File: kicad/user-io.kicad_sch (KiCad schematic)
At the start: 26 parts, among them J1 USB1, SW1 PTS815, U1 MIMXRT1171DVMAB, U2 MAYA-W166-00B, U3 LSM6DSV, U4 LIS2MDL

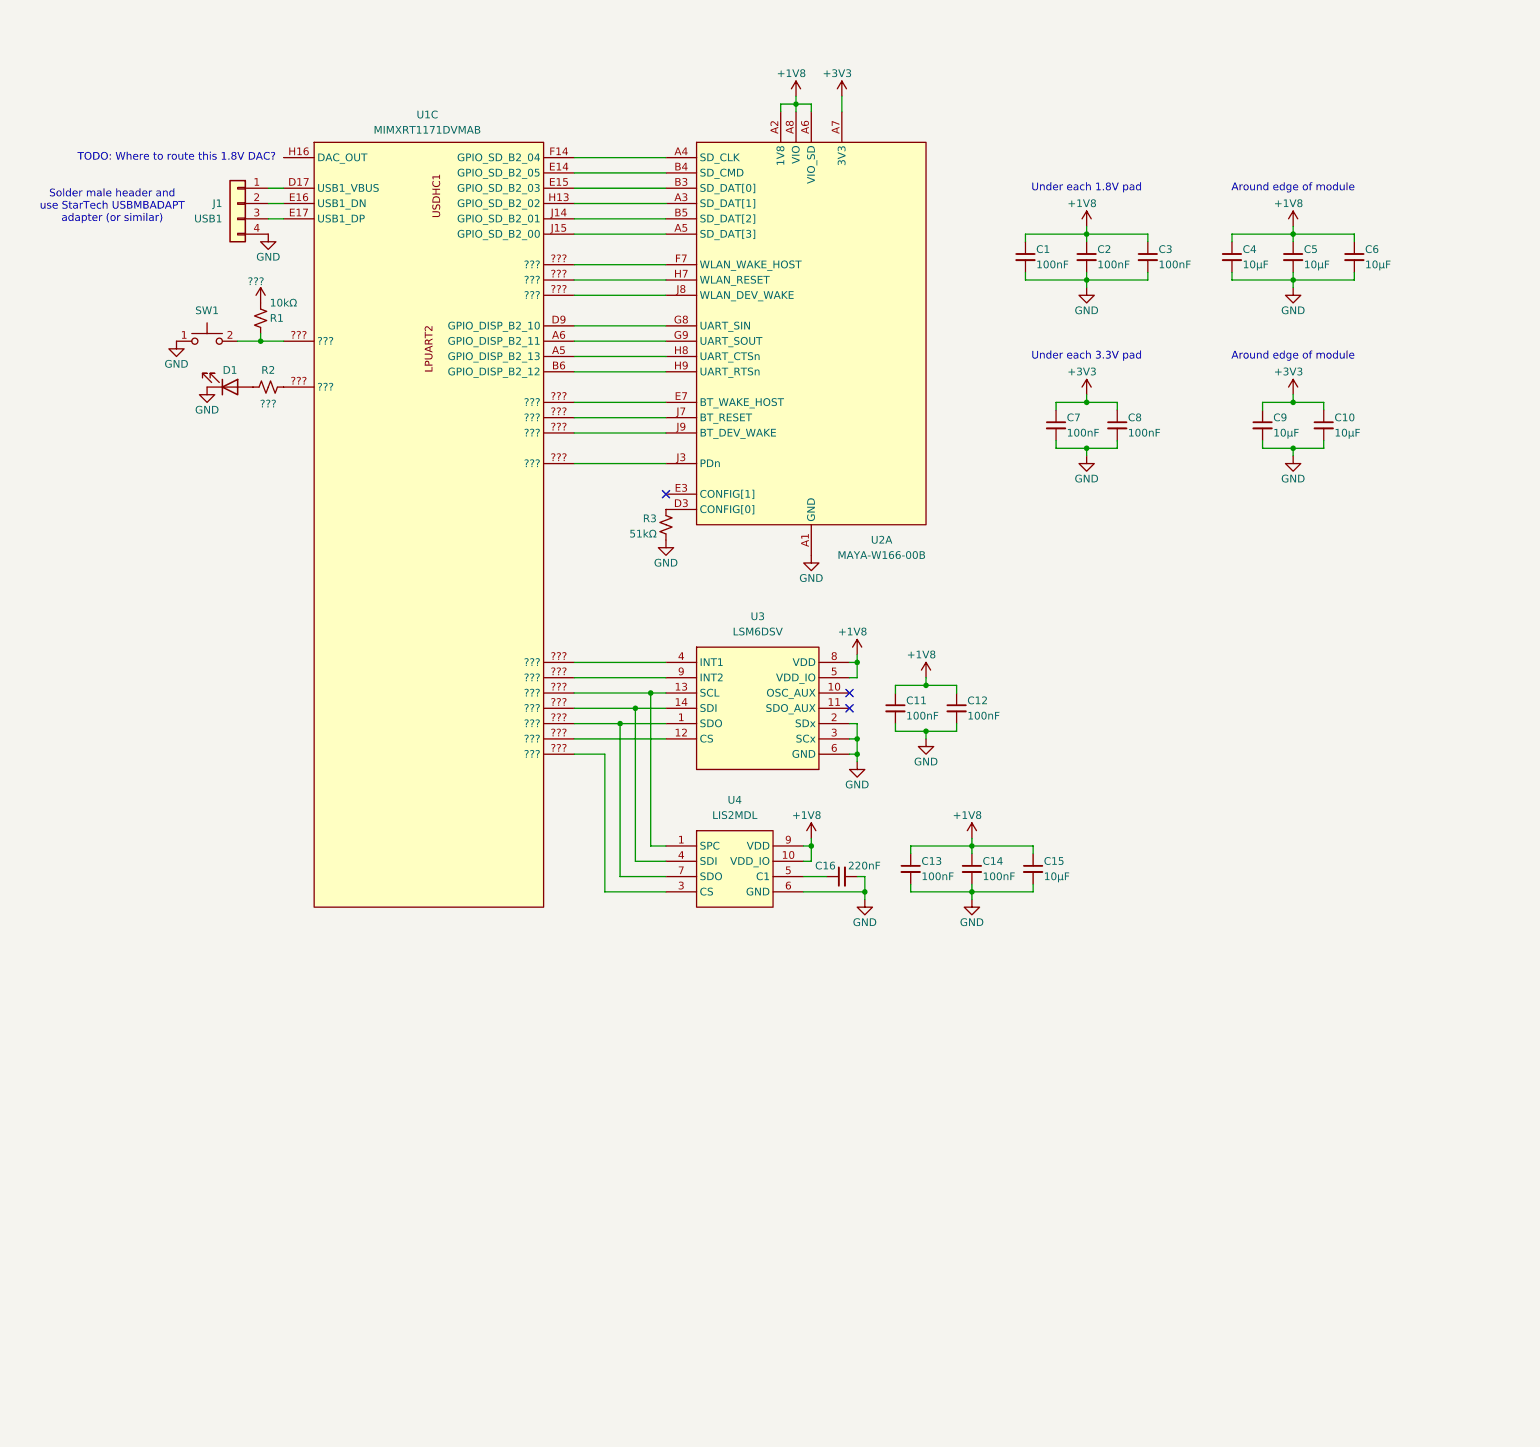
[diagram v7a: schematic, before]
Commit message: added RTMC-G2-4IQ48 to schematic
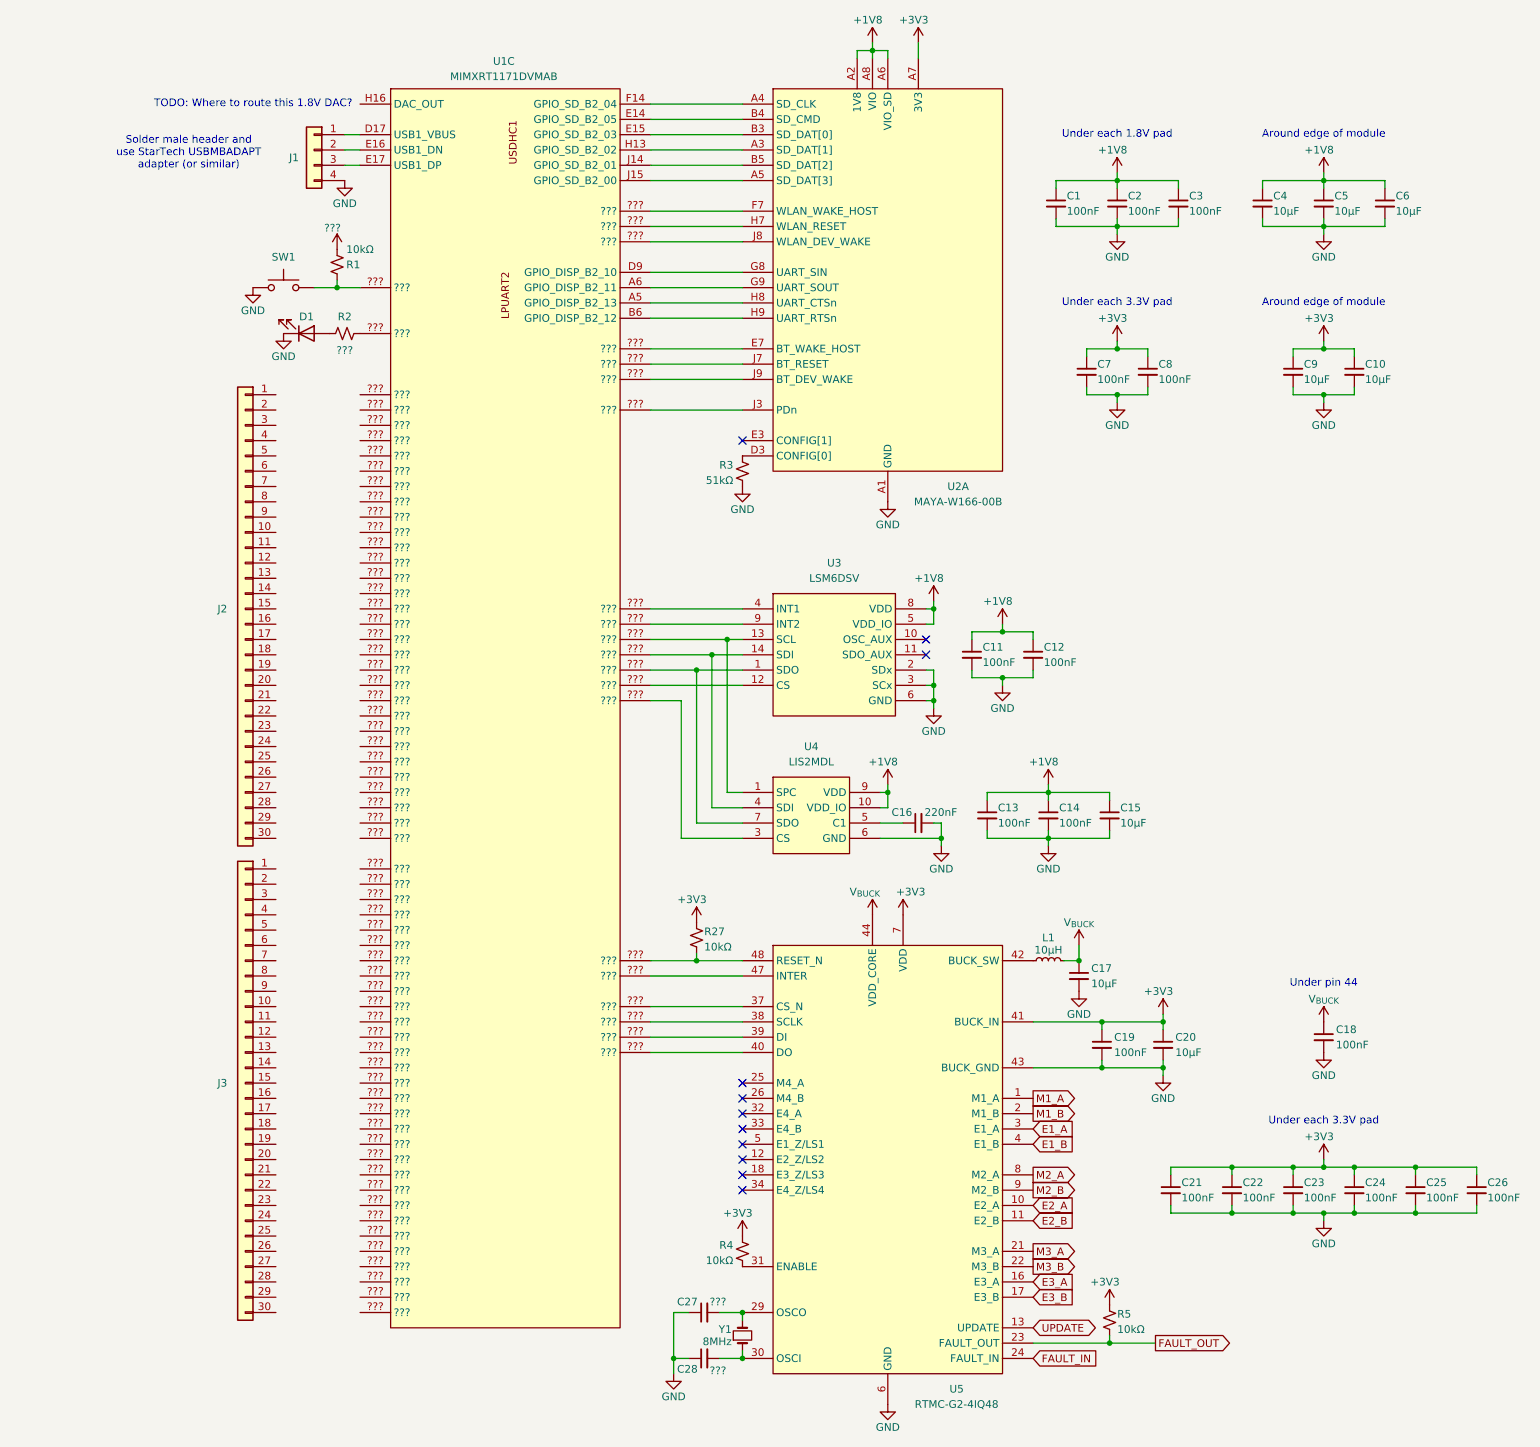
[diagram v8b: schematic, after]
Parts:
- added C17, C20: 10μF, symbol Device:C_Small
- added C18, C19, C21, C22, C23, C24, C25, C26: 100nF, symbol Device:C_Small
- added C27, C28: ???, symbol Device:C_Small
- added J2, J3: Conn_01x30, symbol Connector_Generic:Conn_01x30
- added L1: 10μH, symbol Device:L_Small
- added R27, R4, R5: 10kΩ, symbol Device:R_Small_US
- added U5: RTMC-G2-4IQ48, symbol project_symbols:RTMC-G2-4IQ48
- added Y1: 8MHz, symbol Device:Crystal_Small
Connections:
- net +3V3: now also C19.1, C20.1, C21.1, C22.1, C23.1, C24.1, C25.1, C26.1, R27.1, R4.1, R5.1, U5.15 (VDD), U5.20 (VDD), U5.28 (VDD), U5.36 (VDD), U5.41 (BUCK_IN), U5.46 (VDD), U5.7 (VDD)
- net GND: now also C17.2, C18.2, C19.2, C20.2, C21.2, C22.2, C23.2, C24.2, C25.2, C26.2, C27.1, C28.1, U5.14 (GND), U5.19 (GND), U5.27 (GND), U5.35 (GND), U5.43 (BUCK_GND), U5.45 (GND), U5.6 (GND)
- new net: C27.2, U5.29 (OSCO), Y1.2
- new net: C28.2, U5.30 (OSCI), Y1.1
- new net: R4.2, U5.31 (ENABLE)
- new net: U1.???, U5.37 (CS_N)
- new net: U1.???, U5.38 (SCLK)
- new net: U1.???, U5.39 (DI)
- new net: U1.???, U5.40 (DO)
- new net: L1.2, U5.42 (BUCK_SW)
- new net: U1.???, U5.47 (INTER)
- new net: R27.2, U1.???, U5.48 (RESET_N)
- new net E1_A: U5.3 (E1_A)
- new net E1_B: U5.4 (E1_B)
- new net E2_A: U5.10 (E2_A)
- new net E2_B: U5.11 (E2_B)
- new net E3_A: U5.16 (E3_A)
- new net E3_B: U5.17 (E3_B)
- new net FAULT_IN: U5.24 (FAULT_IN)
- new net FAULT_OUT: R5.2, U5.23 (FAULT_OUT)
- new net M1_A: U5.1 (M1_A)
- new net M1_B: U5.2 (M1_B)
- new net M2_A: U5.8 (M2_A)
- new net M2_B: U5.9 (M2_B)
- new net M3_A: U5.21 (M3_A)
- new net M3_B: U5.22 (M3_B)
- new net UPDATE: U5.13 (UPDATE)
- new net V_{BUCK}: C17.1, C18.1, L1.1, U5.44 (VDD_CORE)
- no-connect marks 3 -> 11
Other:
- note added: "Under pin 44"
- moved on the sheet: C1, C10, C11, C12, C13, C14, C15, C16, C2, C3, C4, C5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
